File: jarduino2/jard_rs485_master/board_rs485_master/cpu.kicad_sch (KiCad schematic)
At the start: 8 parts, among them J2 Log, J6 Button, U1 RtcArduino

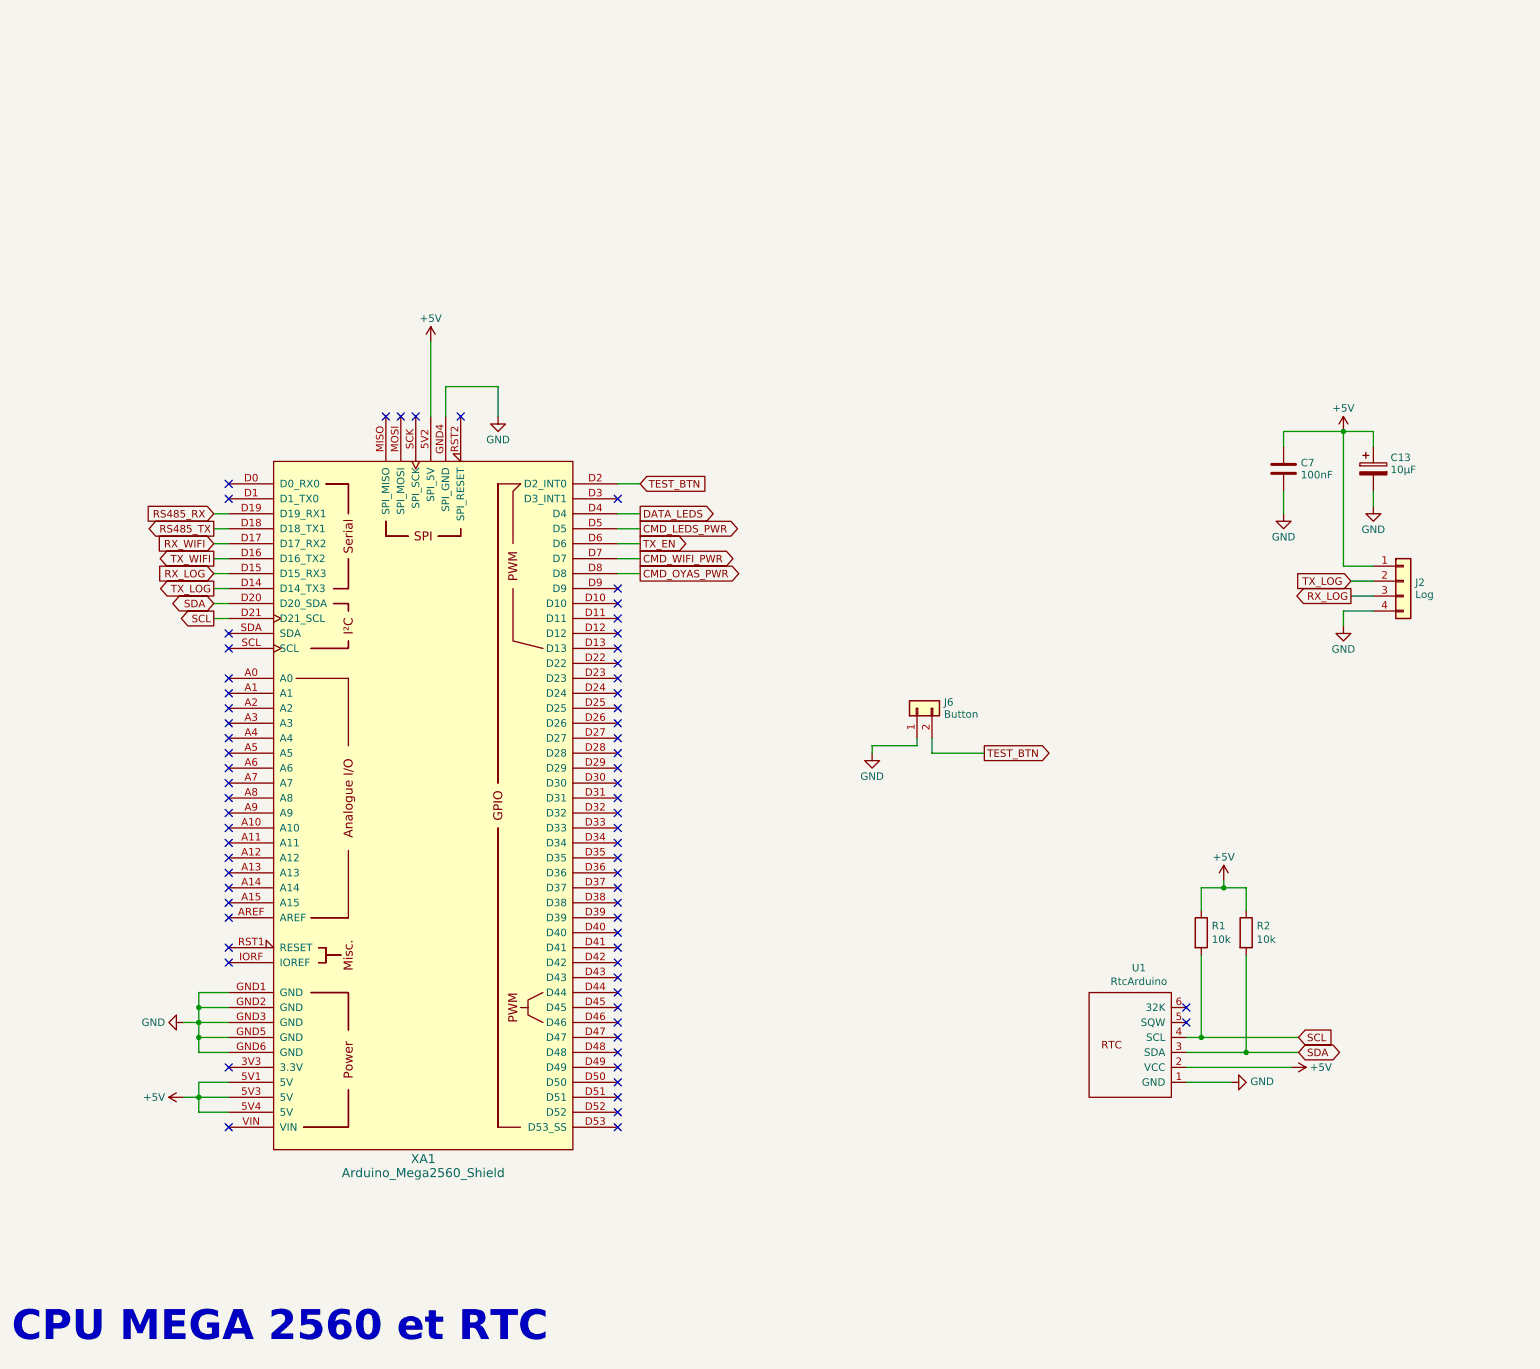
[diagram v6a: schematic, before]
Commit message: Réaffactation des commandes PWR de Wifi et LEDs (compatibilité soft) + suppression de la sheet Wifi sur le schéma (regreoupé dans UC)
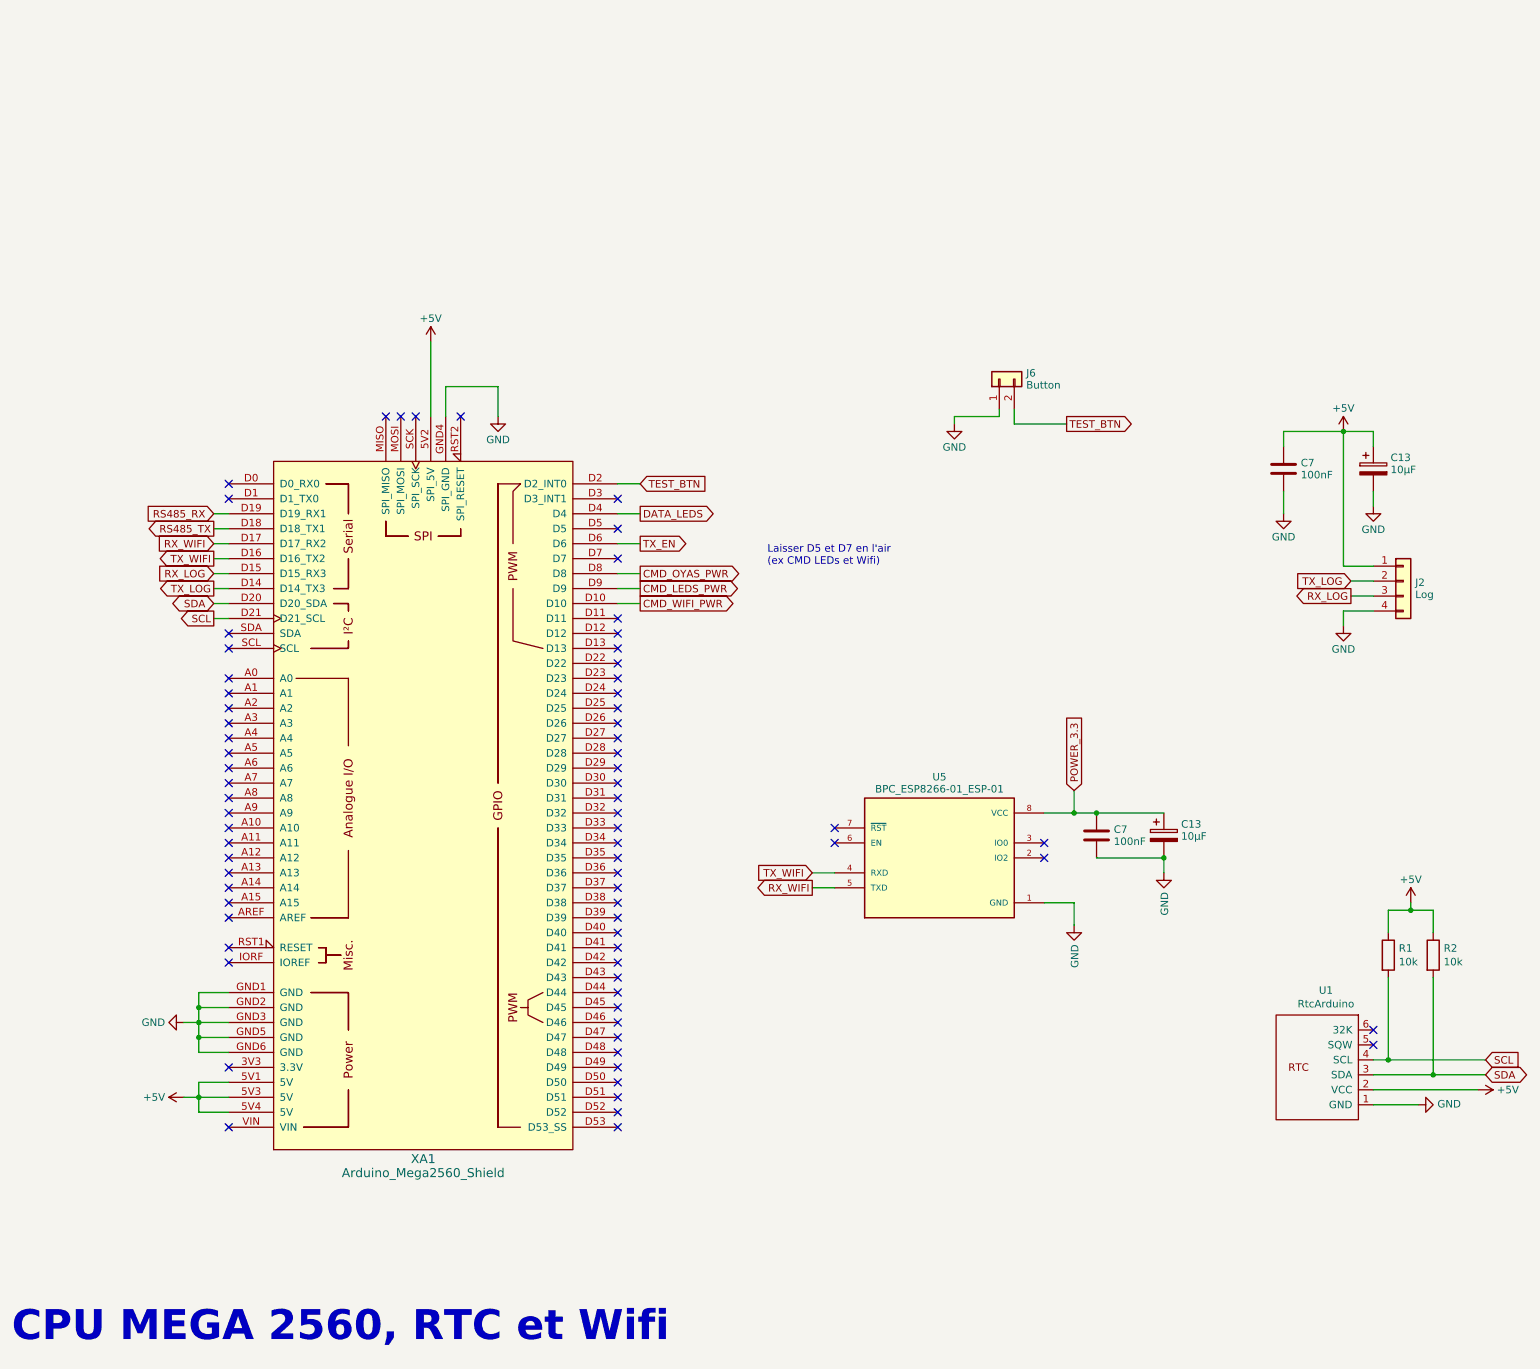
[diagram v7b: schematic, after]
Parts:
- added C13: 10µF, Capacitor_THT:CP_Radial_D4.0mm_P2.00mm, symbol Device:C_Polarized
- added C7: 100nF, Capacitor_THT:C_Disc_D5.0mm_W2.5mm_P2.50mm, symbol Device:C
- added U5: BPC_ESP8266-01_ESP-01, bpc:BPC_XCVR_ESP8266-01_ESP-01, symbol bpc:BPC_ESP8266-01_ESP-01
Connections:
- net CMD_LEDS_PWR: now also XA1.D9; no longer XA1.D5
- net CMD_WIFI_PWR: now also XA1.D10; no longer XA1.D7
- net GND: now also C13.2, C7.2, U5.1 (GND)
- net RX_WIFI: now also U5.5 (TXD)
- net TX_WIFI: now also U5.4 (RXD)
- new net POWER_3.3: C13.1, C7.1, U5.8 (VCC)
- no-connect marks 69 -> 73
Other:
- note added: "CPU MEGA 2560, RTC et Wifi"
- note added: "Laisser D5 et D7 en l'air (ex CMD LEDs et Wifi)"
- note removed: "CPU MEGA 2560 et RTC"
- moved on the sheet: J6, R1, R2, U1
